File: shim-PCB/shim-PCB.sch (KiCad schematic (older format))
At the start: 29 parts, among them J1 ROMI-Encoder, J10 LineSensor, J11 LineSensor, J12 SPI, J13 Ultrasonic., J14 THING, J15 THING, J16 ROMI, J17 i2c, J18 ROMI, J2 ROMI-Encoder, J3 Conn_01x19_Female, J4 ServoAnalog, J5 Conn_01x19_Female, J6 Conn_01x19_Female, J7 ROMI, J8 ROMI, J9 Conn_01x19_Female

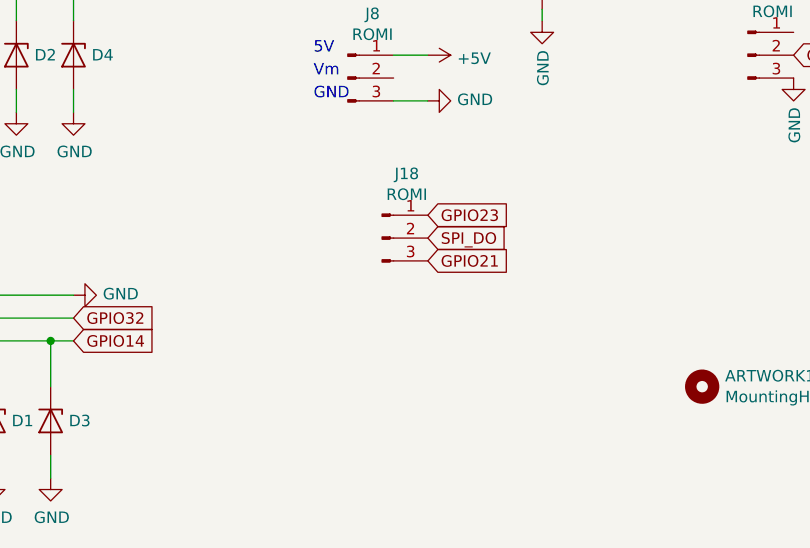
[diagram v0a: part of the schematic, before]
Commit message: gpio 23/21 select is now a jumper.
#33
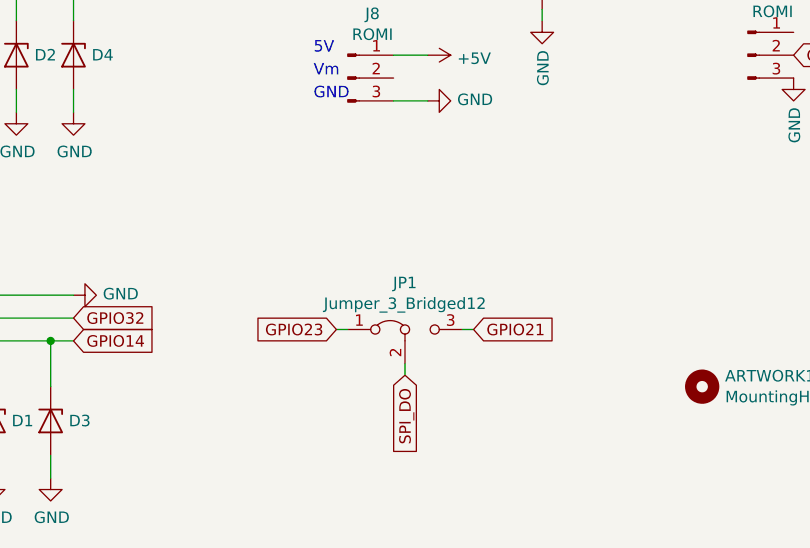
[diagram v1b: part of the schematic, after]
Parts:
- removed J18: ROMI, Connector_PinSocket_2.54mm:PinSocket_1x03_P2.54mm_Vertical, symbol Connector:Conn_01x03_Male
- added JP1: Jumper_3_Bridged12, Jumper:SolderJumper-3_P1.3mm_Bridged12_RoundedPad1.0x1.5mm, symbol Jumper:Jumper_3_Bridged12
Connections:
- wire segments 160 -> 163
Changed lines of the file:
@@
 Text Notes 8650 2900 0    50   ~ 0
 Free: 23 22 21 19 18 5
-$Comp
-L Connector:Conn_01x03_Male J18
-U 1 1 5F126D8C
-P 3400 6150
-F 0 "J18" H 3508 6431 50  0000 C CNN
-F 1 "ROMI" H 3508 6340 50  0000 C CNN
-F 2 "Connector_PinSocket_2.54mm:PinSocket_1x03_P2.54mm_Vertical" H 3400 6150 50  0001 C CNN
-F 3 "~" H 3400 6150 50  0001 C CNN
-	1    3400 6150
-	1    0    0    -1
-$EndComp
-Text GLabel 3600 6050 2    50   Input ~ 0
+Text GLabel 3200 6550 0    50   Input ~ 0
 GPIO23
-Text GLabel 3600 6250 2    50   Input ~ 0
+Text GLabel 3800 6550 2    50   Input ~ 0
 GPIO21
 Text GLabel 6350 1000 2    50   Input ~ 0
 SPI_DO
-Text GLabel 3600 6150 2    50   Input ~ 0
+Text GLabel 3500 6750 3    50   Input ~ 0
 SPI_DO
 $Comp
@@
 Wire Wire Line
 	5600 950  5600 1000
+$Comp
+L Jumper:Jumper_3_Bridged12 JP1
+U 1 1 5F229CDD
+P 3500 6550
+F 0 "JP1" H 3500 6754 50  0000 C CNN
+F 1 "Jumper_3_Bridged12" H 3500 6663 50  0000 C CNN
+F 2 "Jumper:SolderJumper-3_P1.3mm_Bridged12_RoundedPad1.0x1.5mm" H 3500 6550 50  0001 C CNN
+F 3 "~" H 3500 6550 50  0001 C CNN
+	1    3500 6550
+	1    0    0    -1
+$EndComp
+Wire Wire Line
+	3800 6550 3750 6550
+Wire Wire Line
+	3500 6700 3500 6750
+Wire Wire Line
+	3250 6550 3200 6550
 $EndSCHEMATC

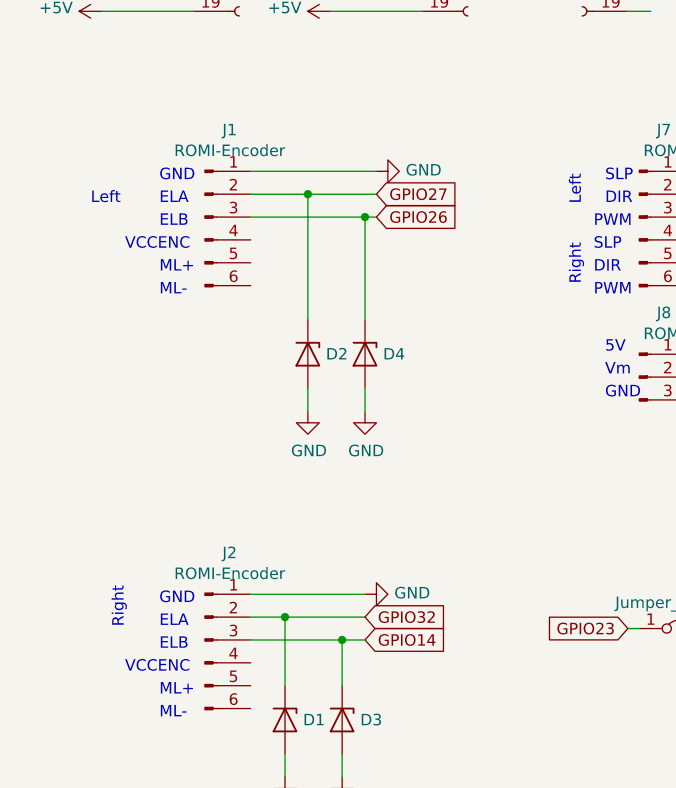
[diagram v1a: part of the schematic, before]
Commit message: Swapped 26/27
#39
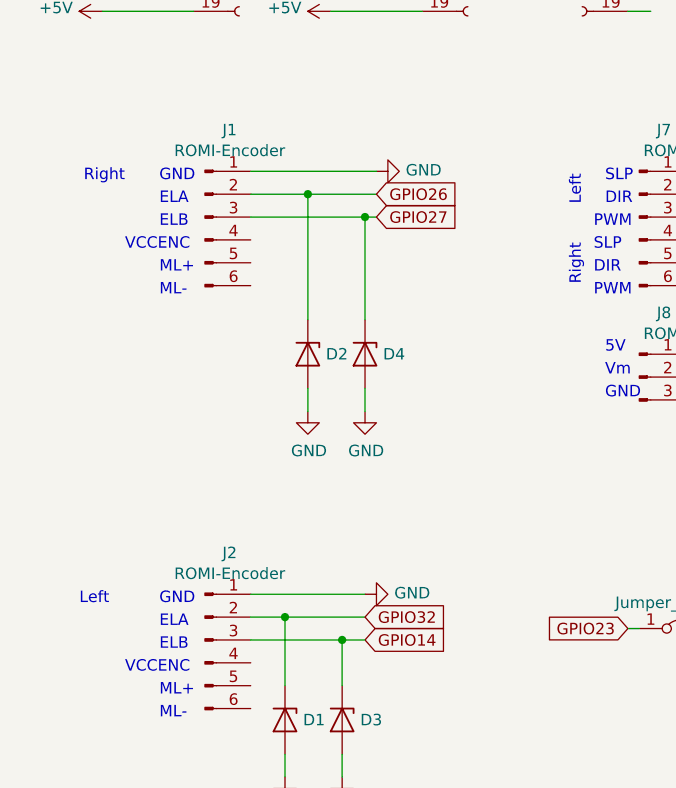
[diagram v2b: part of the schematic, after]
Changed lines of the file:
@@
 	0    -1   -1   0
 $EndComp
+Text GLabel 2100 4750 2    50   Input ~ 0
+GPIO27
 Text GLabel 2100 4650 2    50   Input ~ 0
-GPIO27
-Text GLabel 2100 4750 2    50   Input ~ 0
 GPIO26
 Text GLabel 5100 1400 2    50   Input ~ 0
@@
 Text Notes 3000 4700 1    50   ~ 0
 Left
-Text Notes 850  4700 0    50   ~ 0
+Text Notes 800  6450 0    50   ~ 0
 Left
-Text Notes 1000 6550 1    50   ~ 0
+Text Notes 1000 4600 2    50   ~ 0
 Right
 $Comp

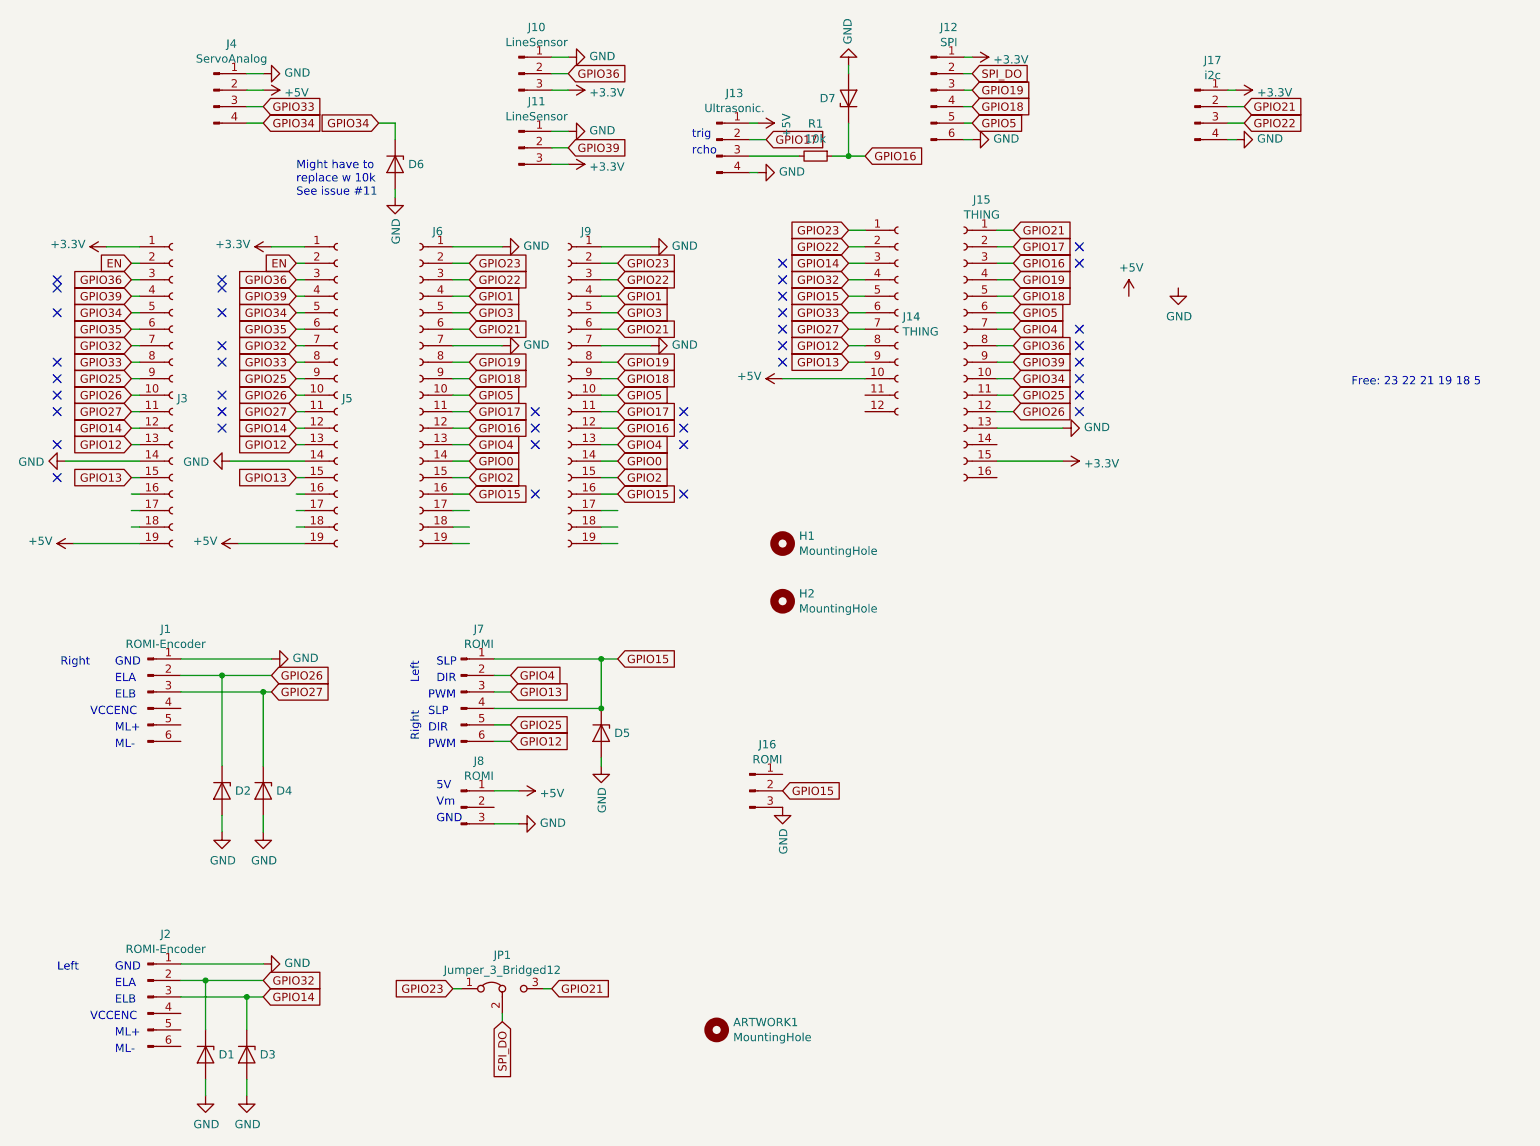
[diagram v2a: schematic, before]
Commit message: Jumper switches SDA between 21/23 defaulting to 21
resolved issue #41
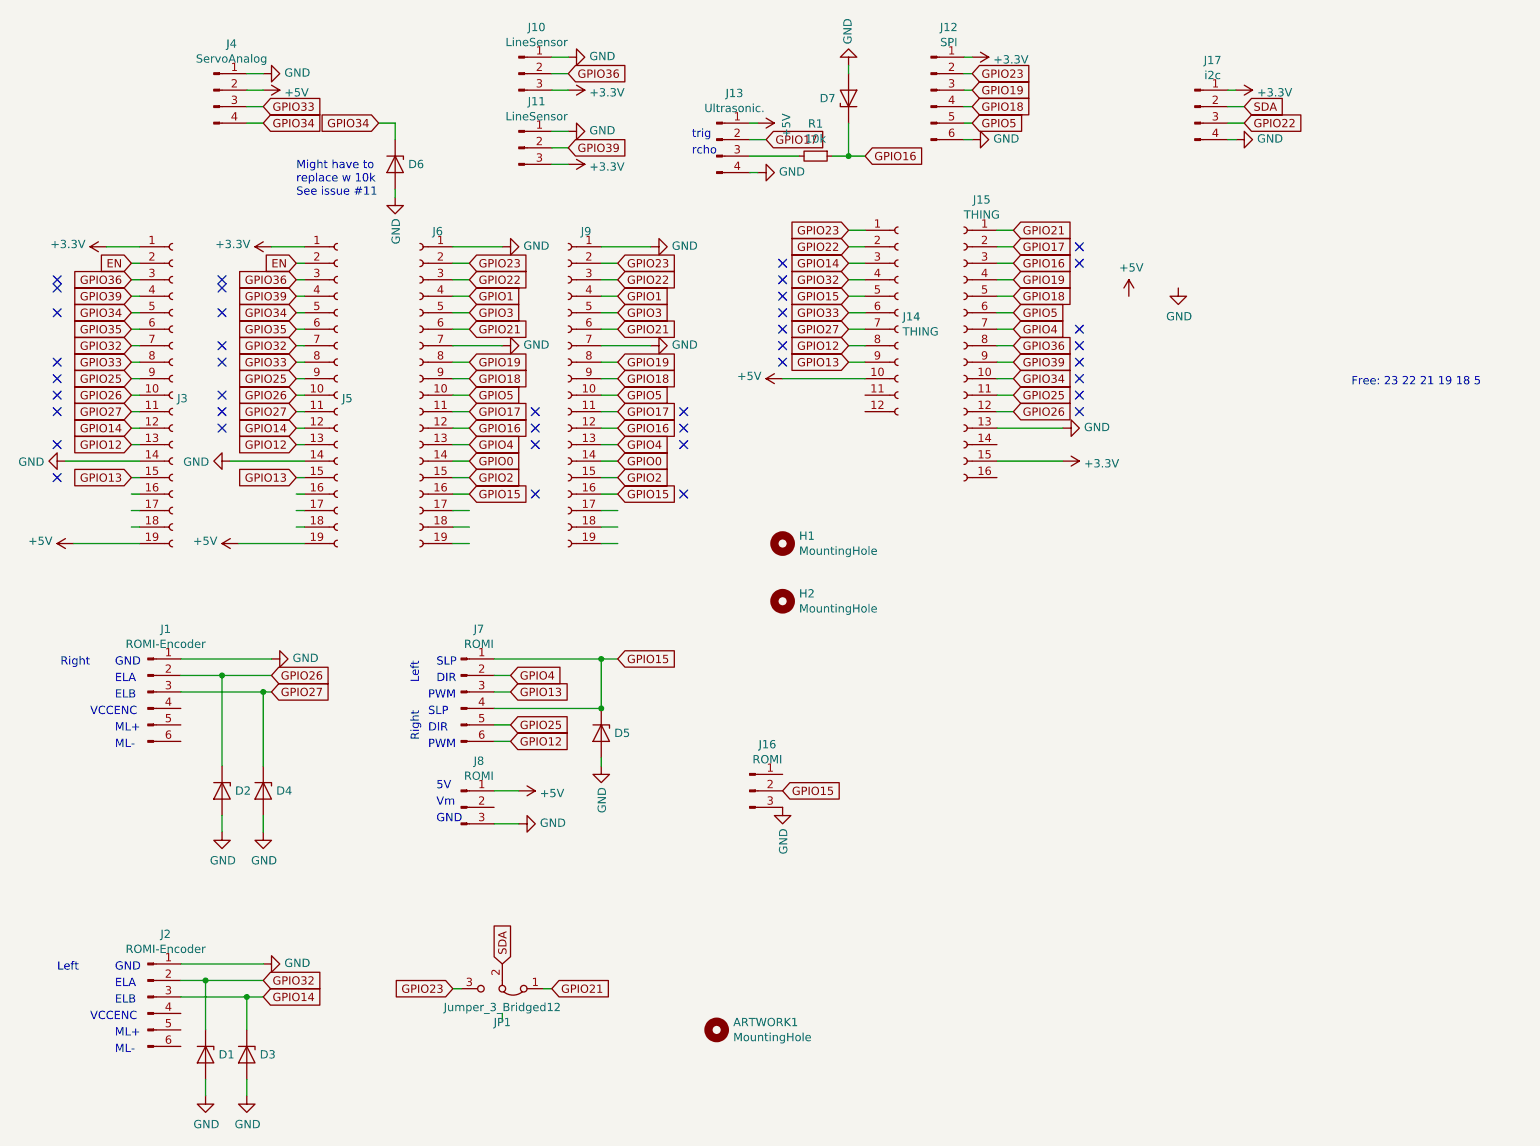
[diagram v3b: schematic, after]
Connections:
- net labels added: SDA
- net labels removed: SPI_DO
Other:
- moved on the sheet: JP1
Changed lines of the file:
@@
 Wire Wire Line
 	7950 1400 7900 1400
-Text GLabel 8000 1200 2    50   Input ~ 0
-GPIO21
 Text GLabel 8000 1300 2    50   Input ~ 0
 GPIO22
@@
 Text GLabel 3800 6550 2    50   Input ~ 0
 GPIO21
-Text GLabel 6350 1000 2    50   Input ~ 0
-SPI_DO
-Text GLabel 3500 6750 3    50   Input ~ 0
-SPI_DO
 $Comp
 L Mechanical:MountingHole ARTWORK1
@@
 F 3 "~" H 3500 6550 50  0001 C CNN
 	1    3500 6550
-	1    0    0    -1
+	-1   0    0    1
 $EndComp
 Wire Wire Line
@@
 Wire Wire Line
 	3250 6550 3200 6550
+Text GLabel 6350 1000 2    50   Input ~ 0
+GPIO23
+Text GLabel 8000 1200 2    50   Input ~ 0
+SDA
+Text GLabel 3500 6400 1    50   Input ~ 0
+SDA
 $EndSCHEMATC
